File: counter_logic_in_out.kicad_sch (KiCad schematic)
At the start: 15 parts

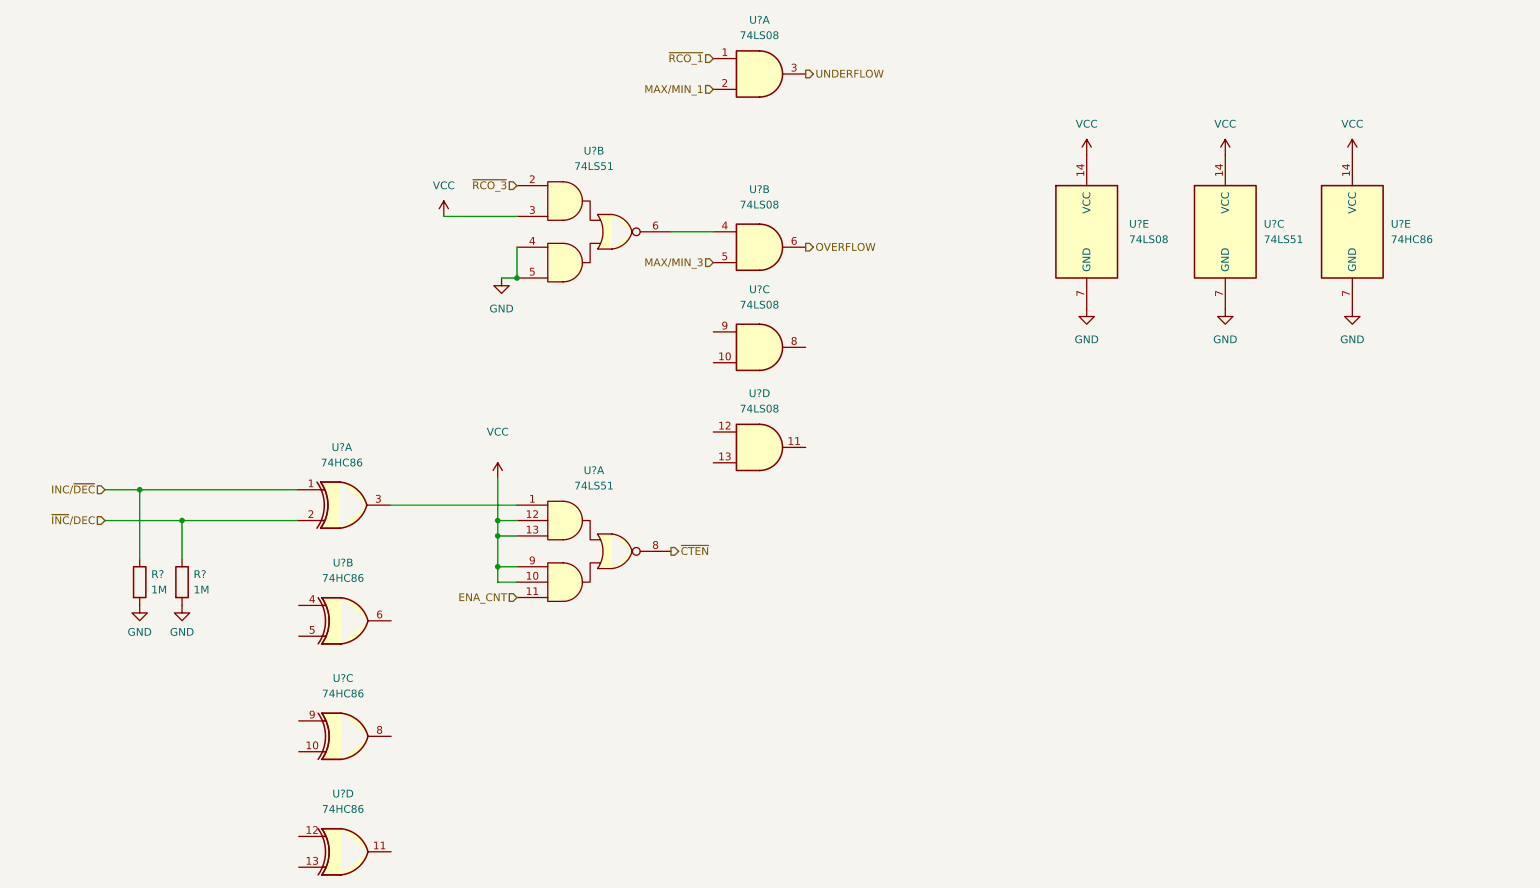
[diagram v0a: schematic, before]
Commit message: Review fixes
- swapped to HC components
- removed ctn_enable
- all 12 LEDs merged into 1 sheet
- No more error with the electrical checker
- various style improvements
- Introduce sleep deprivation errors like calling tranceivers d flip flops
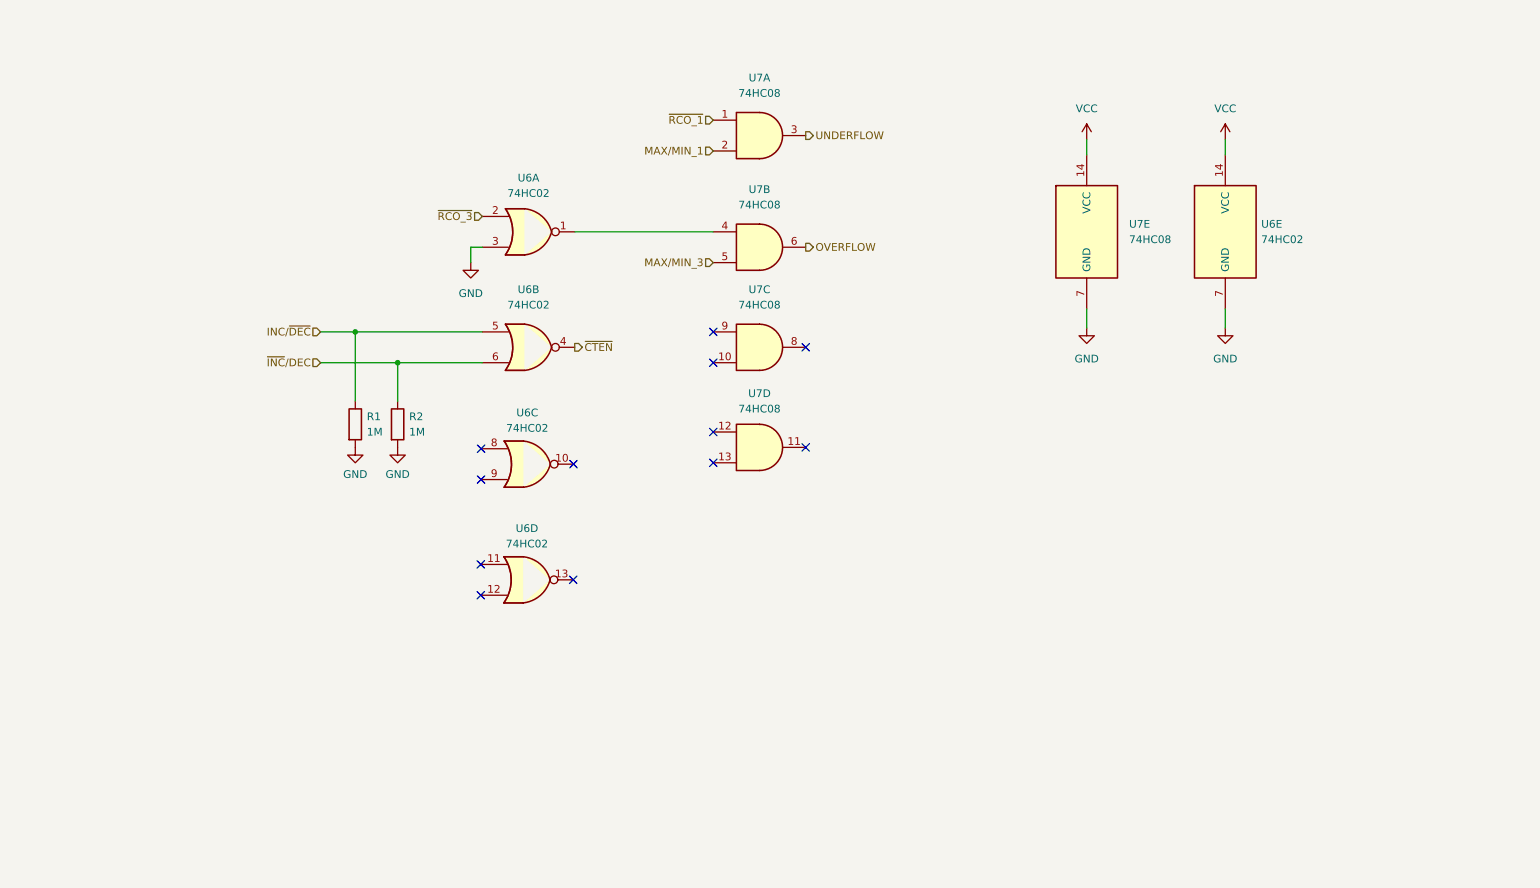
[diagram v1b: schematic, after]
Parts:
- removed U? (x5): 74HC86, symbol 74xx:74HC86
- removed U? (x3): 74LS51, symbol 74xx:74LS51
- added U6: 74HC02, symbol 74xx:74HC02
- U7: renamed from U?; value 74LS08 -> 74HC08
- U7: renamed from U?; value 74LS08 -> 74HC08; symbol 74xx:74LS08 -> 74xx:74HC08
- gave numbers to parts that had none: 2
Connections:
- net GND: now also U6.3, U6.7 (GND)
- net INC/~{DEC}: now also U6.5
- net VCC: now also U6.14 (VCC)
- net ~{CTEN}: now also U6.4
- net ~{INC}/DEC: now also U6.6
- net ~{RCO_3}: now also U6.2
- net at U7.4: now also U6.1
- no-connect marks 0 -> 12
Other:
- moved on the sheet: R1, R2, U7A

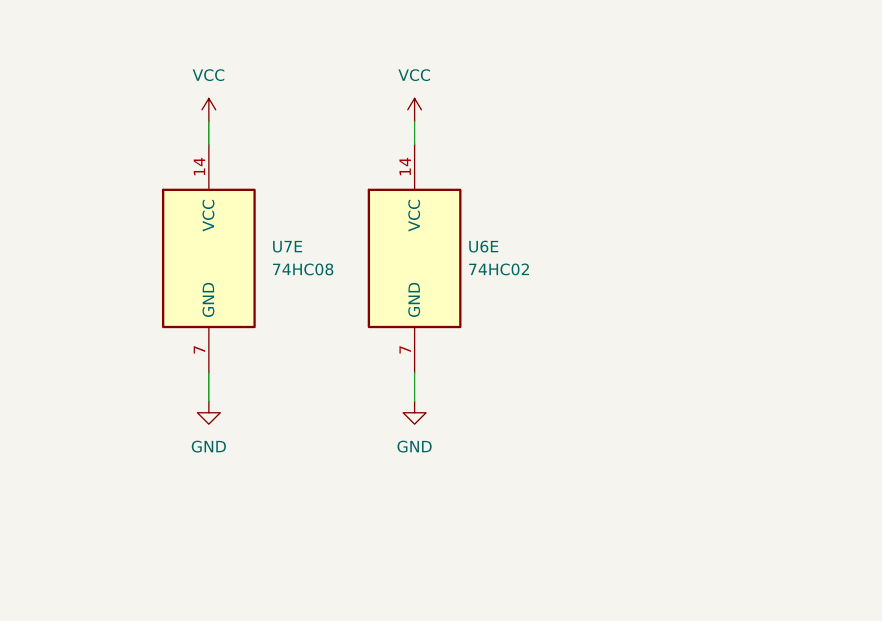
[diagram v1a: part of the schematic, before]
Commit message: Add edge cuts
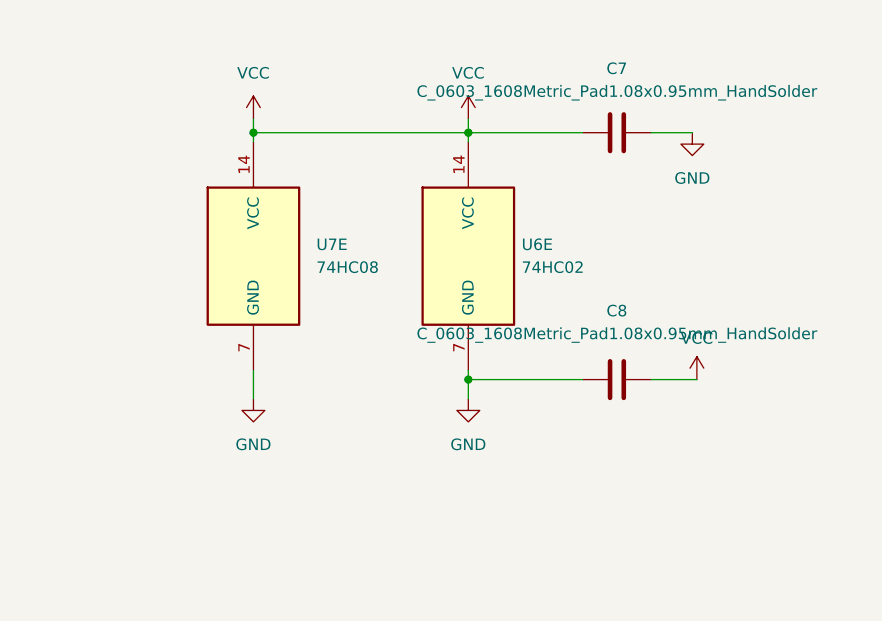
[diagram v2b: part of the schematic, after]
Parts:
- added C7, C8: C_0603_1608Metric_Pad1.08x0.95mm_HandSolder, Capacitor_SMD:C_0603_1608Metric_Pad1.08x0.95mm_HandSolder, symbol Device:C
- R1, R2: footprint (none) -> Resistor_SMD:R_1206_3216Metric_Pad1.30x1.75mm_HandSolder
- U6: footprint (none) -> Package_SO:SOIC-14_3.9x8.7mm_P1.27mm; Component (none) -> SN74HC02DR
- U7: footprint (none) -> Package_SO:SOIC-14_3.9x8.7mm_P1.27mm
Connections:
- net GND: now also C7.2, C8.1
- net VCC: now also C7.1, C8.2
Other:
- moved on the sheet: U6E, U7E

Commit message: routed and pretty
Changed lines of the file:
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@@
     (in_bom yes) (on_board yes) (fields_autoplaced)
     (property "Reference" "C7" (id 0) (at 244.094 43.688 90))
-    (property "Value" "C_0603_1608Metric_Pad1.08x0.95mm_HandSolder" (id 1) (at 244.094 46.228 90))
+    (property "Value" "C_0603_1608Metric_Pad1.08x0.95mm_HandSolder" (id 1) (at 244.094 46.228 90)
+      (effects (font (size 1.27 1.27)) hide)
+    )
     (property "Footprint" "Capacitor_SMD:C_0603_1608Metric_Pad1.08x0.95mm_HandSolder" (id 2) (at 247.904 49.8348 0)
       (effects (font (size 1.27 1.27)) hide)
@@
     (in_bom yes) (on_board yes) (fields_autoplaced)
     (property "Reference" "C8" (id 0) (at 244.094 70.612 90))
-    (property "Value" "C_0603_1608Metric_Pad1.08x0.95mm_HandSolder" (id 1) (at 244.094 73.152 90))
+    (property "Value" "C_0603_1608Metric_Pad1.08x0.95mm_HandSolder" (id 1) (at 244.094 73.152 90)
+      (effects (font (size 1.27 1.27)) hide)
+    )
     (property "Footprint" "Capacitor_SMD:C_0603_1608Metric_Pad1.08x0.95mm_HandSolder" (id 2) (at 247.904 77.2668 0)
       (effects (font (size 1.27 1.27)) hide)
